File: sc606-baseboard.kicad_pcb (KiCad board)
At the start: 6 copper layers, 100 x 90 mm, 462 parts, among them IC1 TPS54561DPRT, IC2 TPS7A0518PDBVT, IC3 HD3SS3220, IC4 HD3SS3220, J1 PJ-202A, J10 WE_632723300011, J11 USB-A3-C31-D-RA-CS1, J12 U_FL-R-SMT-1_10_, J13 USB-A3-C31-D-RA-CS1, J2 WE_68715014522, J3 F52R-1A7H1-11020, J4 46756-1001, J5 U_FL-R-SMT-1_10_, J6 U_FL-R-SMT-1_10_, J7 DM3AT-SF-PEJM5, J8 693022010811, J9 0473460001, M1 SC606T, Q1 BSS138APW, Q2 BSS138-7-F, Q3 BSS138APW, Q4 BSS138APW, Q5 BSS138APW, Q6 BSS138APW, Q7 BSS138-7-F, Q8 BSS138-7-F, SW1 1X03, U1 AP62301WU-7, U10 NCP163ASN330T1G, U11 EMIF06-MSD02N16, U12 FSUSB30MUX, U13 FT232RQ-REEL, U15 USB57442G, U2 AP62301WU-7, U3 AP62301WU-7, U4 74LVC1G123GN, U5 NTS0102GT, U6 PCA9547BS, U7 LT9611UXC, U8 NTS0102GT, U9 TPD13S523PWR, Y1 ABM8G-24.000MHZ-18-D2Y-T, Y2 ABM8G-25.000MHZ-B4Y-T

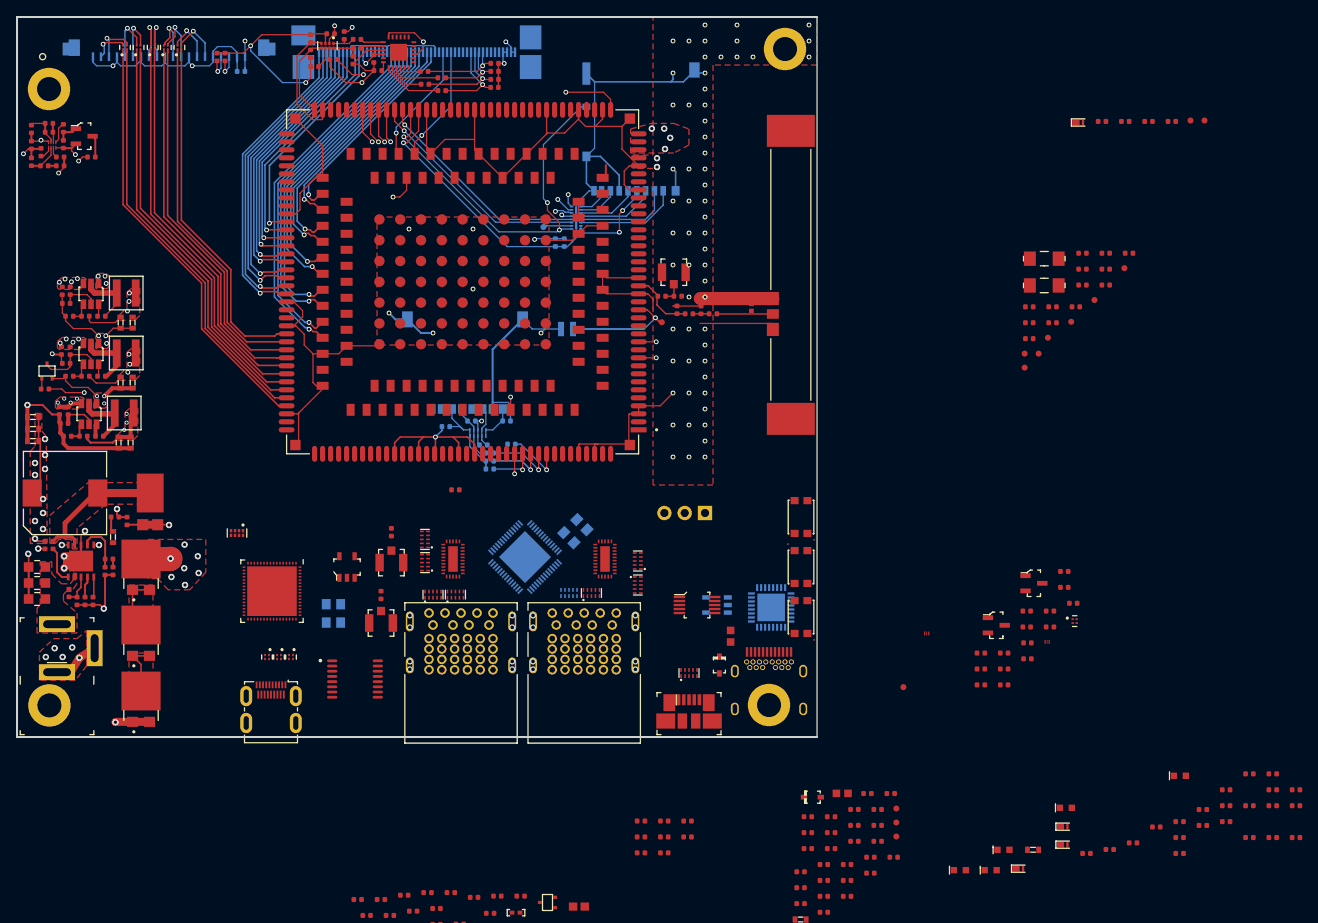
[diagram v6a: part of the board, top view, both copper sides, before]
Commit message: Added USB BOOT, placed USR LEDs and buttons, connected Test Points
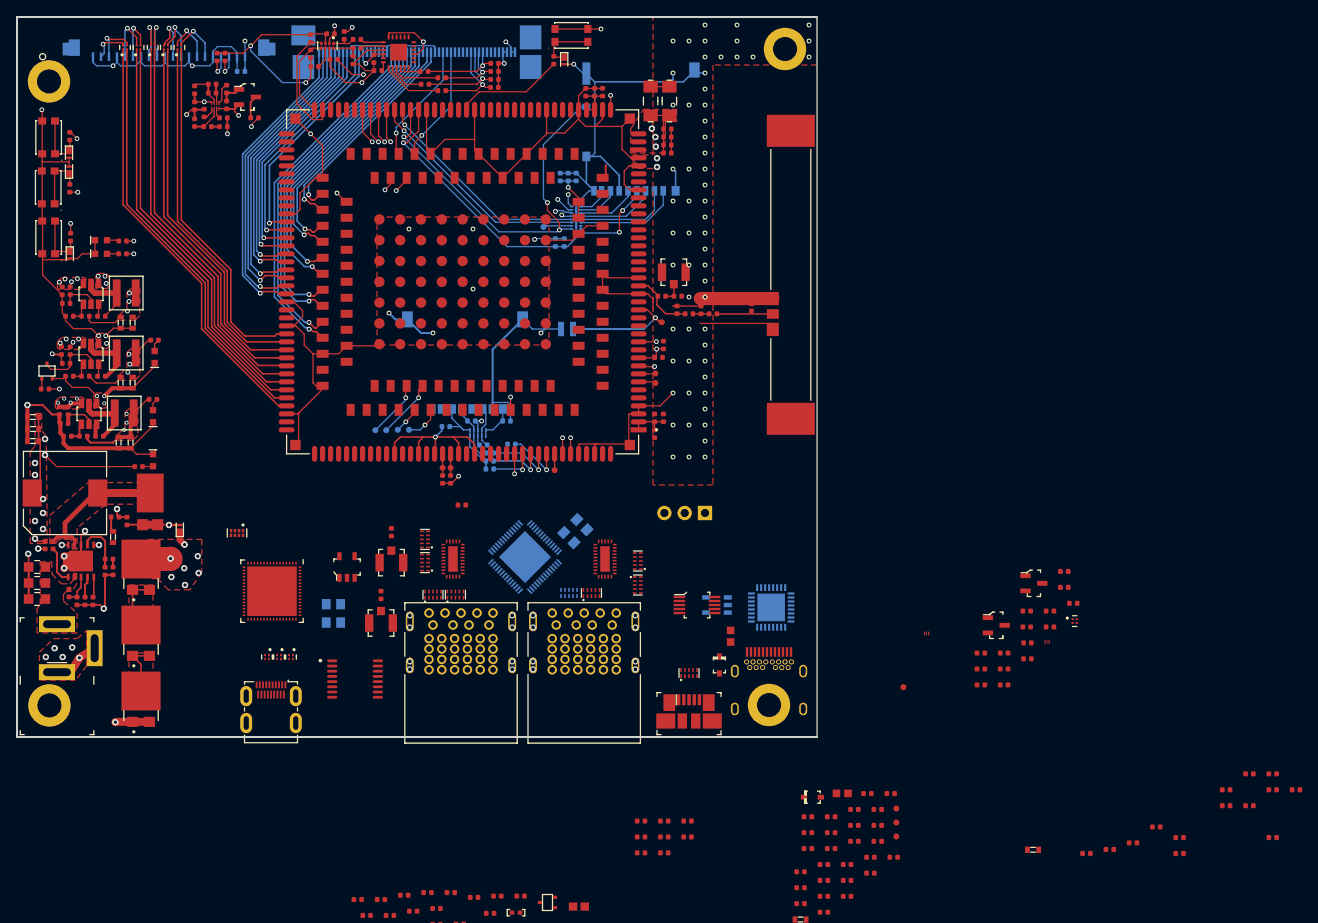
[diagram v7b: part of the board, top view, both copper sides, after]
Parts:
- added D33: PTVS5V0Z1USKPYL, sc606-baseboard-footprints:SOD-964, F.Cu at (143.4, 45.3)
- added R162: R_10k_0402, antmicro-footprints:0402-res, F.Cu at (142.1, 45.4)
- added S4: KMR2, sc606-baseboard-footprints:SW_SPST_4.2x2.8, F.Cu at (144.3, 42.3)
- C11, C14, C16, TP5, TP6, TP7, TP8: moved to B.Cu
- moved R95 173.4 mm to (81.6, 61.4), turned to 90 degrees
- moved R97 171.5 mm to (81.6, 54.9), turned to 270 degrees
- moved R96 168.9 mm to (81.7, 67.5), turned to 270 degrees
- moved R103 153.5 mm to (88.2, 68.0), turned to 180 degrees
- moved R106 151.4 mm to (92.2, 80.4)
- moved D15 150.6 mm to (85.5, 67.9)
- moved D13 150.1 mm to (81.5, 57.0), turned to 270 degrees
- moved R105 150.0 mm to (88.2, 69.6), turned to 180 degrees
- moved D11 147.2 mm to (81.5, 59.3), turned to 90 degrees
- moved D12 144.4 mm to (81.6, 69.6), turned to 270 degrees
- moved R102 143.0 mm to (90.2, 96.2)
- moved R104 140.9 mm to (92.0, 87.8)
- moved D18 135.2 mm to (85.5, 69.6)
- moved D19 127.1 mm to (92.2, 82.5), turned to 90 degrees
- moved D1 123.3 mm to (95.3, 104.1), turned to 90 degrees
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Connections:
- M1 pad 57: Net-(M1-Pad57) -> USB_BOOT
- S1 pad 2: Net-(D11-PadK) -> GND
- S2 pad 2: Net-(D12-PadK) -> GND
- S3 pad 2: Net-(D13-PadK) -> GND
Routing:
- net VOL_DOWN: track 0.00 -> 91.9 mm, vias 0 -> 2
- net VOL_UP: track 0.00 -> 85.8 mm, vias 0 -> 2
- net GND: track 443.5 -> 511.9 mm, vias 99 -> 102
- net 5V0_SYS: track 89.1 -> 142.9 mm, vias 26 -> 25
- net LDO5_1P8: track 0.00 -> 52.8 mm, vias 0 -> 2
- net USR_LED1: track 0.00 -> 41.2 mm, vias 0 -> 2
- net USR_LED2: track 0.00 -> 35.3 mm, vias 0 -> 2
- net LDO6_1P8: track 120.6 -> 151.5 mm, vias 3 -> 4
- net USB_BOOT: track 0.00 -> 13.7 mm
- net CAM_RST: track 57.8 -> 68.1 mm
- net V_SOM: track 82.0 -> 91.2 mm, vias 11 -> 10
- net Net-(M1-Pad248): track 0.00 -> 7.51 mm, vias 0 -> 1
- net Net-(D12-PadK): track 0.00 -> 7.42 mm
- net Net-(D11-PadK): track 0.00 -> 7.41 mm
- net Net-(D13-PadK): track 0.00 -> 7.37 mm
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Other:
- net class CSI_DSI_Inner: clearance 0.15 -> 0.508
- net class CSI_DSI_Outer: clearance 0.15 -> 0.508

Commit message: Prepared layout of USB flash and debug components
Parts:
- C108, L22, R107, U12: moved to B.Cu
- IC2, U13: moved to F.Cu
- moved L22 56.6 mm to (153.4, 97.8), turned to 90 degrees
- moved C108 55.1 mm to (152.0, 97.8), turned to 90 degrees
- moved R107 53.9 mm to (151.0, 97.8), turned to 90 degrees
- moved R110 46.9 mm to (157.2, 116.8)
- moved R108 44.5 mm to (156.8, 118.4), turned to 90 degrees
- moved R109 44.0 mm to (157.2, 115.8)
- moved Q8 41.7 mm to (160.6, 114.6), turned to 180 degrees
- moved C109 41.0 mm to (157.4, 121.0)
- moved C111 39.0 mm to (165.8, 99.8), turned to 270 degrees
- moved C110 38.1 mm to (157.4, 120.0)
- moved Q7 36.9 mm to (160.6, 118.6)
- moved C113 35.7 mm to (171.9, 107.2)
- moved D21 35.0 mm to (168.8, 118.2), turned to 180 degrees
- moved C116 34.2 mm to (172.0, 115.8), turned to 180 degrees
- moved C115 33.6 mm to (171.4, 100.1), turned to 270 degrees
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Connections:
- D21 pad 1: /USB_flash_debug/DBG_USB_D_P -> /USB_flash_debug/DBG_USB_D_N
- D21 pad 2: /USB_flash_debug/DBG_USB_D_N -> /USB_flash_debug/DBG_USB_D_P
